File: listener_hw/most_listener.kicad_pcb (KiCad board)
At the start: 2 copper layers, 122.5 x 78.9 mm, 171 parts, among them J1 1-1394640-1, J2 ANALYSER, J3 I2S, J4 VBAT_IN, J5 PLR135/T10, J6 PLT133/T10W, J7 RCA 75R, J8 LINE L, J9 LINE R, M1 Tang Nano 20K, M2 ESP32-DevKitC-VIE, U1 74LVC1G34, U10 TPS2553DBVR, U11 74LVC1G123, U12 DIR9001, U13 SRC4192, U14 LP5907MFX-3.3, U15 PCM5102A, U16 LP5907MFX-3.3, U17 OPA1678, U18 TPS60403, U2 74LVC1G157, U3 74LVC1G125, U4 74LVC1G123, U5 TPS7B8133DRV, U6 LMR38020F, U7 Si514, U8 LP5907MFX-3.3, U9 74LVC1G79, X1 24.576MHz

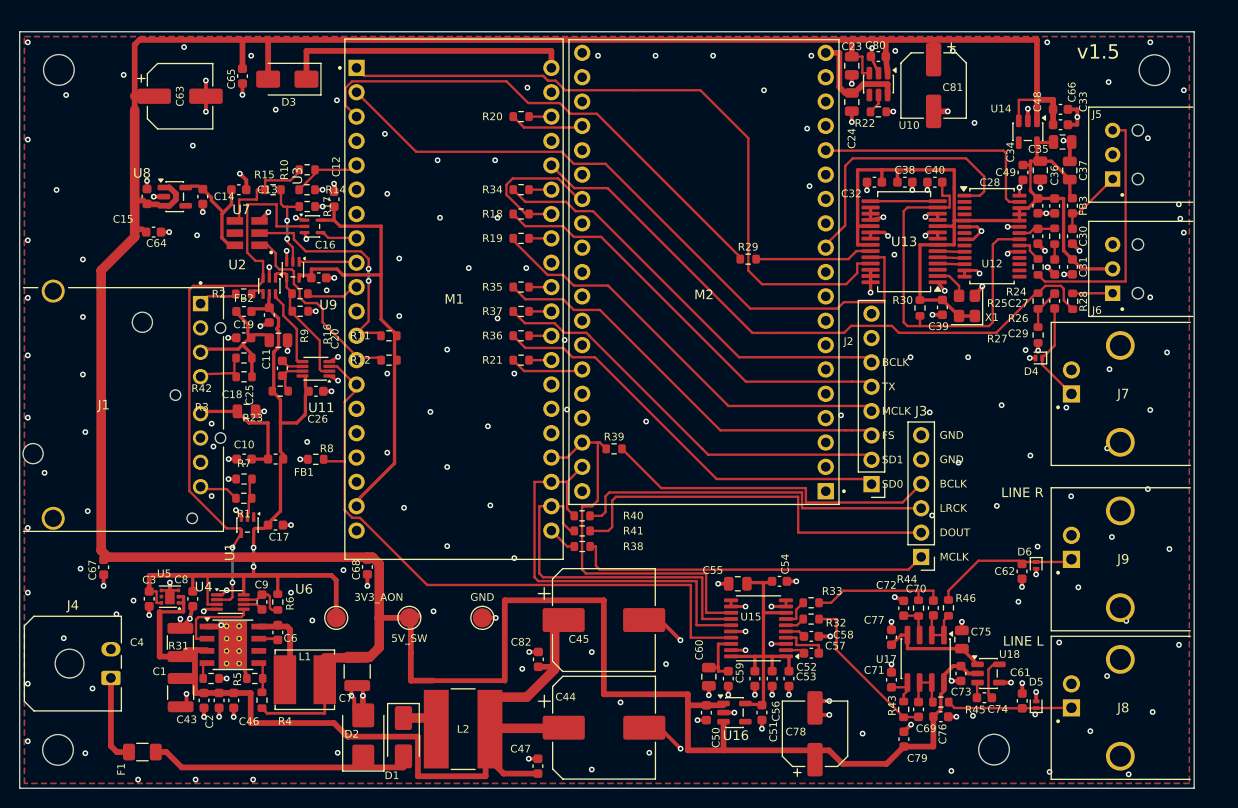
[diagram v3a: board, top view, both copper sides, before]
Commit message: Board v1.6: Cliff TOSLINK jacks, series resistors at their drivers, JLCPCB silk and rotations
- J5/J6: Everlight's PLR135/T10 is no longer made and PLR237/T10BK is not
  stocked, so Cliff's FCR684205R/T (ORJ-5/OTJ-5). Footprint and 3D body from
  Cliff's drawings: pin 1 at the port's right, one peg 3.90 mm in front of the
  pins and two 2.10 mm behind, the body's face on the board's edge. The
  housing is 11.5 mm wide, so J5..J9 and H2 moved about 1.1 mm right (by hand)
  and the board is 123.55 x 78.9 mm.
- The user's moves, routed: R28 turned; R15, R10 and R14 in one row with C13
  and C14 moved; C83 (100 nF 100 V at the TVS behind F1, added to the sheet);
  the series resistors at the pins that drive their lines - J2's six (R18,
  R19, R34..R37) in a column under M2's left edge, R20/R21 at M2's pins 35/25,
  R29 at U13's SDOUT. The loops beside M1's row are gone, UART_TX's branch to
  M2.32 turns up just left of M1's pins, the S/PDIF line moved 1 mm to clear
  R34. The jumpers stay four, 8.8 mm.
- JLCPCB: the CPL rotations are keyed by LCSC part (JLC_TURN), each read off
  the part's EasyEDA footprint; the old table had the electrolytics (C44, C45,
  C63, C78, C81) reversed and U4, U8..U11, U14, U16, U18 a quarter turn off.
  The board itself was never wrong. Silk raised to 1.0/0.15 mm (texts and
  lines) and every reference re-placed beside its part; 32 small parts'
  references are off the silk and stay on F.Fab. make_fab.py refuses thinner
  silk. The stackup (1.6 mm FR-4, 1 oz, ENIG) is in the board and the job file.
- Title block and silk: rev 1.6 of 2026-10-04.

DRC: no error, nothing unconnected, the board matches the sheet.
check_all --quick --strict before this commit: 27 passed; the two steps that
compare with the commit (the generator's files, fab/) are this commit.

Co-Authored-By: Claude Opus 5.5 <noreply@anthropic.com>
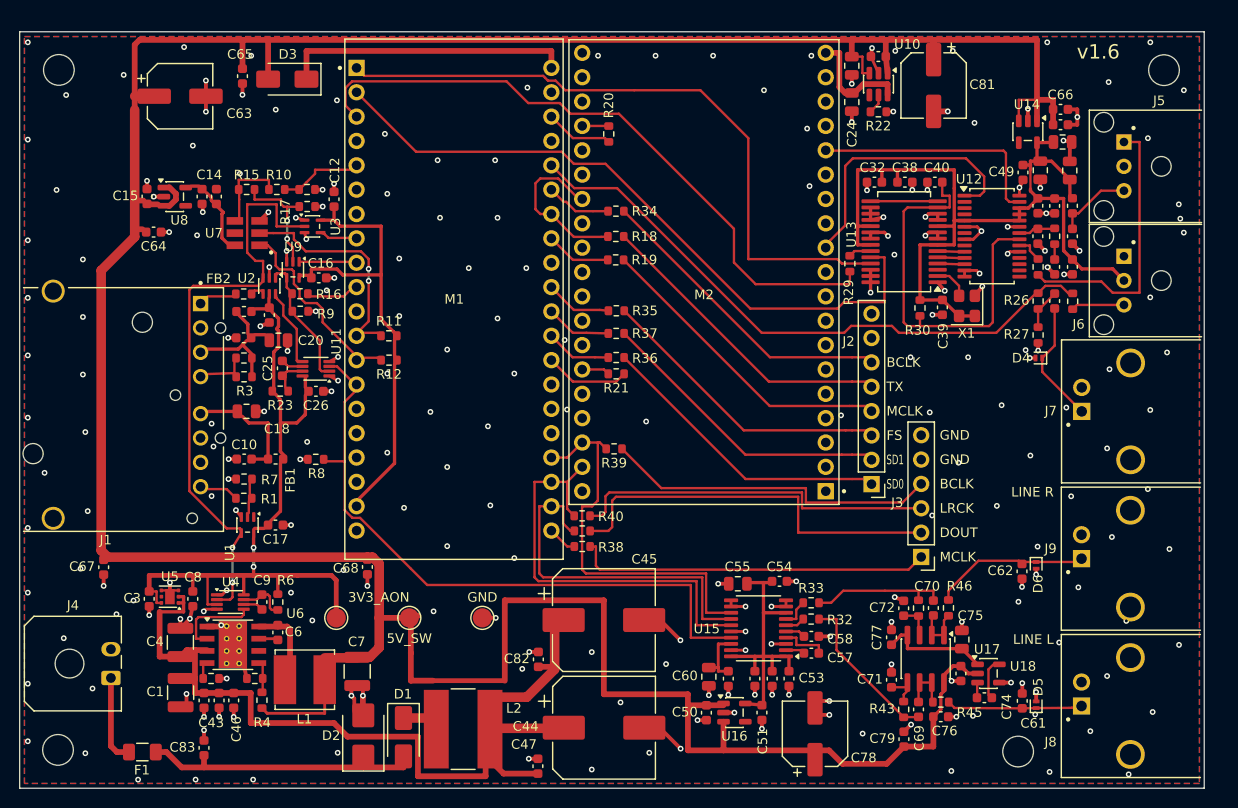
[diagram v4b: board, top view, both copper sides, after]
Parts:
- added C83: 100n 100V, Capacitor_SMD:C_0603_1608Metric, F.Cu at (19.2, 75.8)
- J5: value PLR135/T10 -> FCR684205R; footprint most_listener:Everlight_TOSLINK_T10 -> most_listener:Cliff_TOSLINK_ORJ5_OTJ5
- J6: value PLT133/T10W -> FCR684205T; footprint most_listener:Everlight_TOSLINK_T10 -> most_listener:Cliff_TOSLINK_ORJ5_OTJ5
- moved R29 10.6 mm to (86.6, 25.3), turned to -90 degrees
- moved R35 10.2 mm to (62.2, 30.2), turned to 0 degrees
- moved R37 10.2 mm to (62.2, 32.6), turned to 0 degrees
- moved R36 10.2 mm to (62.2, 35.1), turned to 0 degrees
- moved R18 10.2 mm to (62.2, 22.5), turned to 0 degrees
- moved R34 10.1 mm to (62.2, 19.8), turned to 0 degrees
- moved R19 10.1 mm to (62.2, 24.9), turned to 0 degrees
- moved R21 10.0 mm to (62.2, 36.8)
- moved R20 9.32 mm to (61.4, 11.8), turned to 90 degrees
- moved R10 3.77 mm to (26.8, 17.6)
- moved R15 2.76 mm to (23.7, 17.6)
- moved H4 2.52 mm to (104.1, 76.2)
- moved C13 2.44 mm to (20.5, 18.3), turned to 90 degrees
- moved J7 2.11 mm to (110.8, 40.7)
- moved J5 1.69 mm to (115.2, 15.1)
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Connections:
- J5 pad 1: Net-(J5-VCC) -> Net-(J5-VOUT)
- J5 pad 3: Net-(J5-VOUT) -> Net-(J5-VCC)
- J6 pad 1: Net-(J6-VIN) -> GND
- J6 pad 3: GND -> Net-(J6-VIN)
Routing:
- net /I2S_DIN2_F: track 52.7 -> 68.5 mm
- net Net-(J2-FS): track 43.8 -> 31.2 mm
- net Net-(J2-MCLK): track 45.0 -> 32.4 mm
- net Net-(J2-SD0): track 43.8 -> 31.3 mm
- net Net-(J2-UART_TX): track 44.8 -> 32.3 mm
- net Net-(J2-BCLK): track 44.8 -> 32.4 mm
- net Net-(J2-SD1): track 43.3 -> 31.3 mm
- net Net-(U13-SDOUT): track 12.3 -> 2.36 mm
- net /I2S_DIN_F: track 2.34 -> 8.85 mm
- net Net-(M2-IO15): track 7.74 -> 2.77 mm
- net Net-(M2-IO21): track 7.74 -> 2.91 mm
- net /UART_RX_F: track 2.34 -> 7.07 mm
- net /FS_F: track 2.34 -> 6.95 mm
- net /SD0_F: track 2.34 -> 6.87 mm
- net /SD1_F: track 2.34 -> 6.86 mm
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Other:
- board size 122.5 x 78.9 mm -> 123.5 x 78.9 mm
- board text added: "v1.6"
- board text removed: "v1.5"
